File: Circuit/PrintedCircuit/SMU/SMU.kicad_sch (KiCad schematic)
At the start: 20 parts, among them J1 Conn_01x07_Pin, J2 Conn_01x03_Pin, U1 MCP4922, U2 MCP1501-20xCH, U6 MCP3204

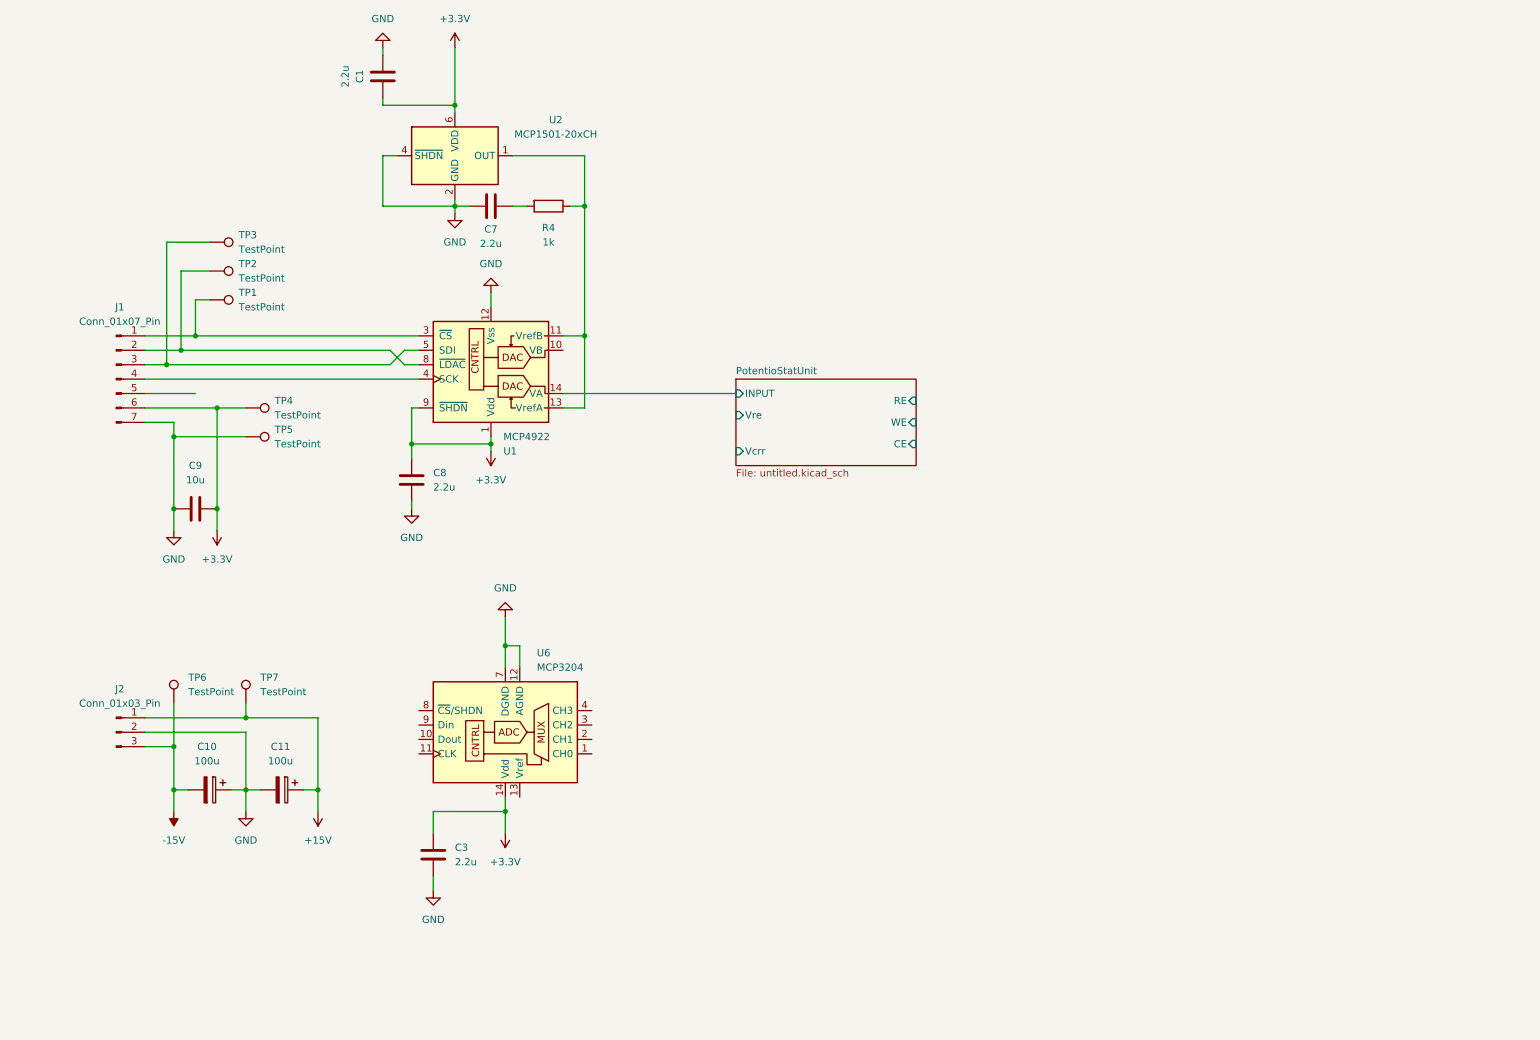
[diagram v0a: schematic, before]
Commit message: 保護回路のシミュレーションを追加
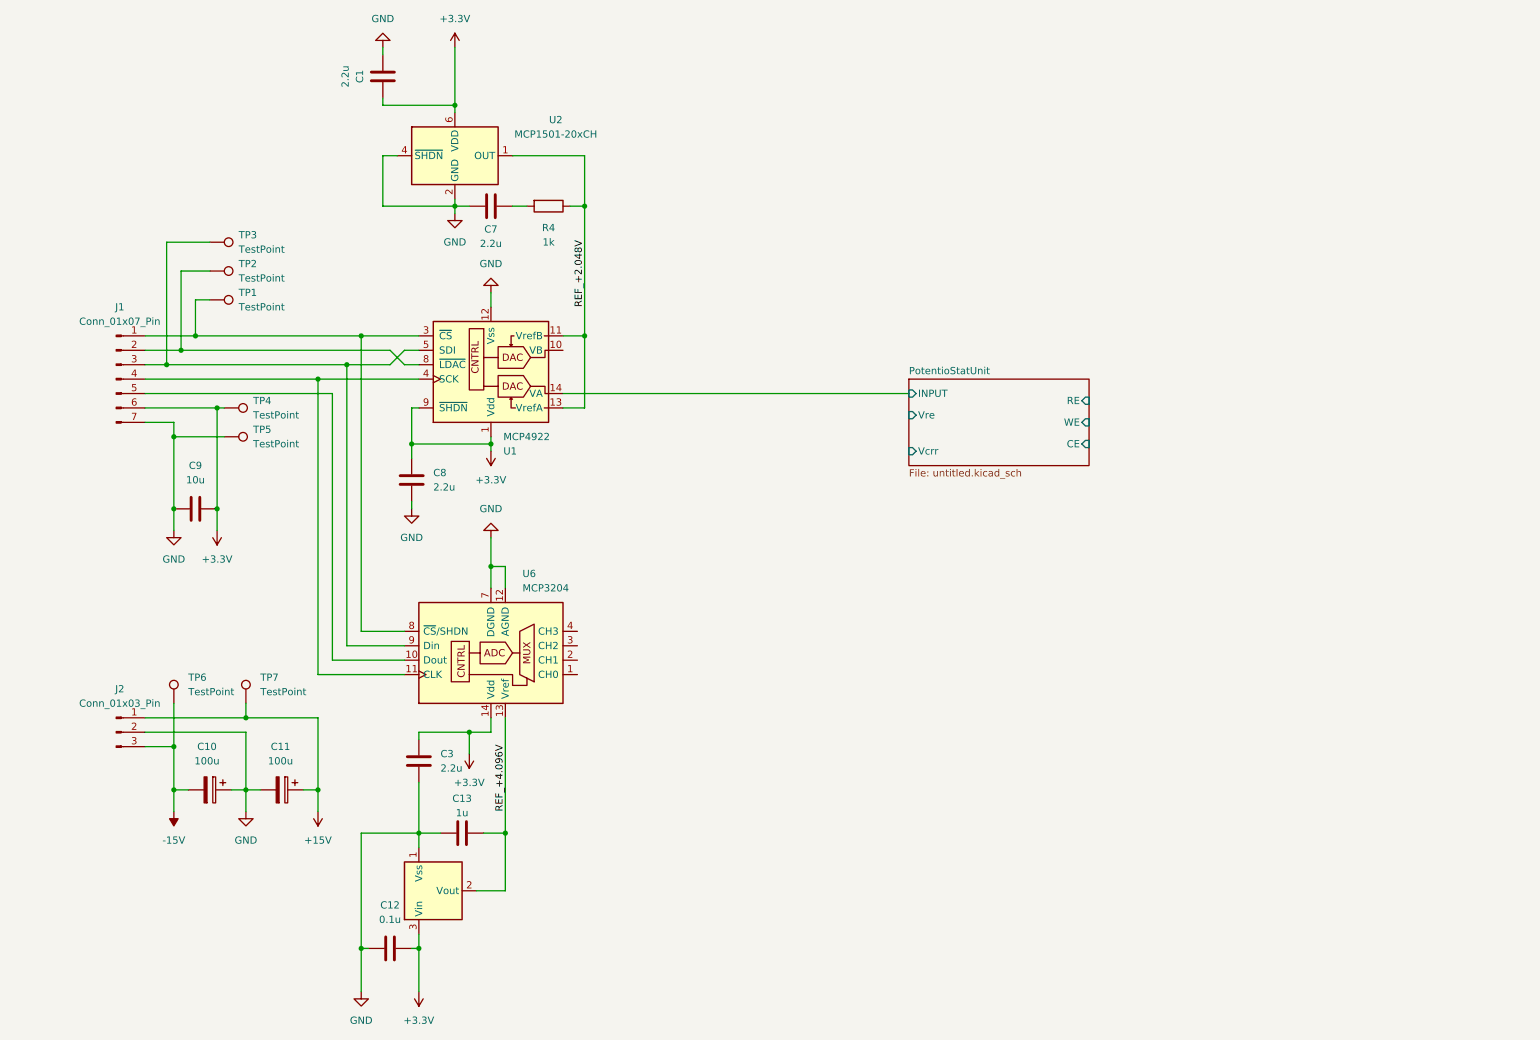
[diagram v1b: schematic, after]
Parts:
- added C12: 0.1u, symbol Device:C
- added C13: 1u, symbol Device:C
- added U7: MCP1541-TO, Package_TO_SOT_THT:TO-92_Inline, symbol Reference_Voltage:MCP1541-TO
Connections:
- net +3.3V: now also C12.2, U7.3 (Vin)
- net GND: now also C12.1, C13.1, U7.1 (Vss)
- net at U6.10 (Dout): now also J1.5 (Pin_5)
- net at U6.11 (CLK): now also J1.4 (Pin_4), U1.4 (SCK)
- net REF_+4.096V: now reaches U6.13 (Vref)
- net REF_+4.096V: now also C13.2, U7.2 (Vout)
- net at U6.8 (~{CS}/SHDN): now also J1.1 (Pin_1), TP1.1, U1.3 (~{CS})
- net at U6.9 (Din): now also J1.3 (Pin_3), TP3.1, U1.5 (SDI)
- net REF_+2.048V: now reaches R4.1, U1.11 (VrefB), U1.13 (VrefA), U2.1 (OUT)
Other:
- moved on the sheet: C3, TP4, TP5, U6

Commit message: SMUのプリント基板回路図完成
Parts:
- removed J1: Conn_01x07_Pin, symbol Connector:Conn_01x07_Pin
- added J1: Conn_01x08_Pin, symbol Connector:Conn_01x08_Pin
- added J3, J4, J5, J6: Conn_Coaxial, symbol Connector:Conn_Coaxial
- added SW1, SW2: SW_SPDT, symbol Switch:SW_SPDT
- added TP8: SPI_SCK, symbol Connector:TestPoint
- added TP9: SPI_RX, symbol Connector:TestPoint
- TP1: value TestPoint -> CS0
- TP2: value TestPoint -> CS1
- TP3: value TestPoint -> SPI_TX
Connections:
- net +3.3V: now also J1.7 (Pin_7)
- net GND: now also J1.8 (Pin_8)
- net PotentioStatUnit/CE: now also J5.2 (Ext), J6.2 (Ext)
- net PotentioStatUnit/RE: now also J5.1 (In), SW2.1 (A)
- net PotentioStatUnit/WE: now also SW2.2 (B)
- net 反転回路/OUTPUT: now reaches U6.1 (CH0)
- net at U6.10 (Dout): now also J1.6 (Pin_6), TP9.1
- net at U1.4 (SCK), U6.11 (CLK): now also J1.5 (Pin_5), TP8.1
- net 反転回路1/OUTPUT: now reaches U6.2 (CH1)
- net at TP1.1, U1.3 (~{CS}): now also J1.1 (Pin_1); no longer U6.8 (~{CS}/SHDN)
- net at TP3.1, U1.5 (SDI), U6.9 (Din): now also J1.4 (Pin_4)
- net at TP2.1: now also U6.8 (~{CS}/SHDN), J1.2 (Pin_2); no longer U1.8 (~{LDAC})
- net PotentioStatUnit1/INPUT: now reaches U1.10 (VB)
- new net: J6.1 (In), SW2.3 (C)
- new net: J4.1 (In), SW1.3 (C)
- new net: J1.3 (Pin_3), U1.8 (~{LDAC})
- new net PotentioStatUnit1/CE: J3.2 (Ext), J4.2 (Ext)
- new net PotentioStatUnit1/RE: J3.1 (In), SW1.1 (A)
- new net PotentioStatUnit1/WE: SW1.2 (B)
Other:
- added sheet PotentioStatUnit1 (untitled.kicad_sch)
- added sheet 反転回路 (Inverting.kicad_sch)
- added sheet 反転回路1 (Inverting.kicad_sch)
- moved on the sheet: C9, TP4, TP5

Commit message: フットプリント設定
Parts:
- removed TP7: TestPoint, symbol Connector:TestPoint
- removed TP8: SPI_SCK, symbol Connector:TestPoint
- removed TP9: SPI_RX, symbol Connector:TestPoint
- added J1: Conn_01x07_Pin, Connector_PinHeader_2.54mm:PinHeader_1x08_P2.54mm_Vertical, symbol Connector:Conn_01x07_Pin
- C1: footprint (none) -> Capacitor_SMD:C_0603_1608Metric_Pad1.08x0.95mm_HandSolder
- C2: renamed from C7; footprint (none) -> Capacitor_SMD:C_0603_1608Metric_Pad1.08x0.95mm_HandSolder
- C3: renamed from C8; footprint (none) -> Capacitor_SMD:C_0603_1608Metric_Pad1.08x0.95mm_HandSolder
- C4: renamed from C9; footprint (none) -> Capacitor_SMD:C_0603_1608Metric_Pad1.08x0.95mm_HandSolder
- C5: renamed from C10; footprint (none) -> Capacitor_SMD:C_0603_1608Metric_Pad1.08x0.95mm_HandSolder
- C6: renamed from C11; footprint (none) -> Capacitor_SMD:C_0603_1608Metric_Pad1.08x0.95mm_HandSolder
- C7: renamed from C3; footprint (none) -> Capacitor_SMD:C_0603_1608Metric_Pad1.08x0.95mm_HandSolder
- C8: renamed from C13; footprint (none) -> Capacitor_SMD:C_0603_1608Metric_Pad1.08x0.95mm_HandSolder
- C9: renamed from C12; footprint (none) -> Capacitor_SMD:C_0603_1608Metric_Pad1.08x0.95mm_HandSolder
- J2: renamed from J1; footprint (none) -> Connector_JST:JST_XH_B7B-XH-A_1x07_P2.50mm_Vertical
- J3, J4, J5: footprint (none) -> Connector_Coaxial:BNC_Amphenol_B6252HB-NPP3G-50_Horizontal
- J6: renamed from J2; footprint (none) -> Connector_JST:JST_XH_B3B-XH-A_1x03_P2.50mm_Vertical
- J7: renamed from J6; footprint (none) -> Connector_Coaxial:BNC_Amphenol_B6252HB-NPP3G-50_Horizontal
- R1: renamed from R4; footprint (none) -> Resistor_SMD:R_0603_1608Metric_Pad0.98x0.95mm_HandSolder
- SW1, SW2: footprint (none) -> Button_Switch_THT:SW_Slide-03_Wuerth-WS-SLTV_10x2.5x6.4_P2.54mm
- TP1: value CS0 -> TestPoint; footprint (none) -> Connector_PinHeader_2.54mm:PinHeader_1x01_P2.54mm_Vertical
- TP2: value CS1 -> TestPoint; footprint (none) -> Connector_PinHeader_2.54mm:PinHeader_1x01_P2.54mm_Vertical
- TP3: value SPI_TX -> TestPoint; footprint (none) -> Connector_PinHeader_2.54mm:PinHeader_1x01_P2.54mm_Vertical
- TP4, TP5, TP6: footprint (none) -> Connector_PinHeader_2.54mm:PinHeader_1x01_P2.54mm_Vertical
- U2: renamed from U1; footprint (none) -> Package_DIP:DIP-14_W7.62mm
- U3: renamed from U6; footprint (none) -> Package_DIP:DIP-14_W7.62mm
- renumbered U2 to U1, U7 to U4
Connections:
- net +15V: now also J1.6 (Pin_6)
- net +3.3V: now also J1.4 (Pin_4); no longer TP4.1
- net -15V: now also J1.7 (Pin_7); no longer TP6.1
- net GND: now also J1.5 (Pin_5); no longer TP5.1
- net PotentioStatUnit/INPUT: now also TP2.1
- net PotentioStatUnit/Vcrr: now also TP4.1
- net PotentioStatUnit1/INPUT: now also TP1.1
- net PotentioStatUnit1/Vcrr: now also TP6.1
- net 反転回路/OUTPUT: now also TP3.1
- net 反転回路1/OUTPUT: now also TP5.1
- net at J2.6 (Pin_6), U3.10 (Dout): now also J1.3 (Pin_3)
- net at J2.5 (Pin_5), U2.4 (SCK), U3.11 (CLK): now also J1.2 (Pin_2)
- net at J2.2 (Pin_2), U3.8 (~{CS}/SHDN): no longer TP2.1
- net at J2.4 (Pin_4), U2.5 (SDI), U3.9 (Din): now also J1.1 (Pin_1); no longer TP3.1
- net at J2.1 (Pin_1), U2.3 (~{CS}): no longer TP1.1
- no-connect marks 0 -> 2
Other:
- note added: "+ RE (SMU:-) - CE (SMU:+)"
- note added: "+ WE (SMU:NC) - CE (SMU:-)"
- note added: "1: SMUmode 3: PGSmode"
- note added: "J1 - 1: SPI_TX 2: SPI_SCK 3: SPI_RX 4: +3.3V 5: GND 6: +15V 7: -15V"
- note added: "TP1: INPUT_B TP2: INPUT_A TP3: Vcrr_INV_A TP4: Vcrr_A TP5: Vcrr_INV_B TP6: Vcrr_B"
- moved on the sheet: C5, C6, J6

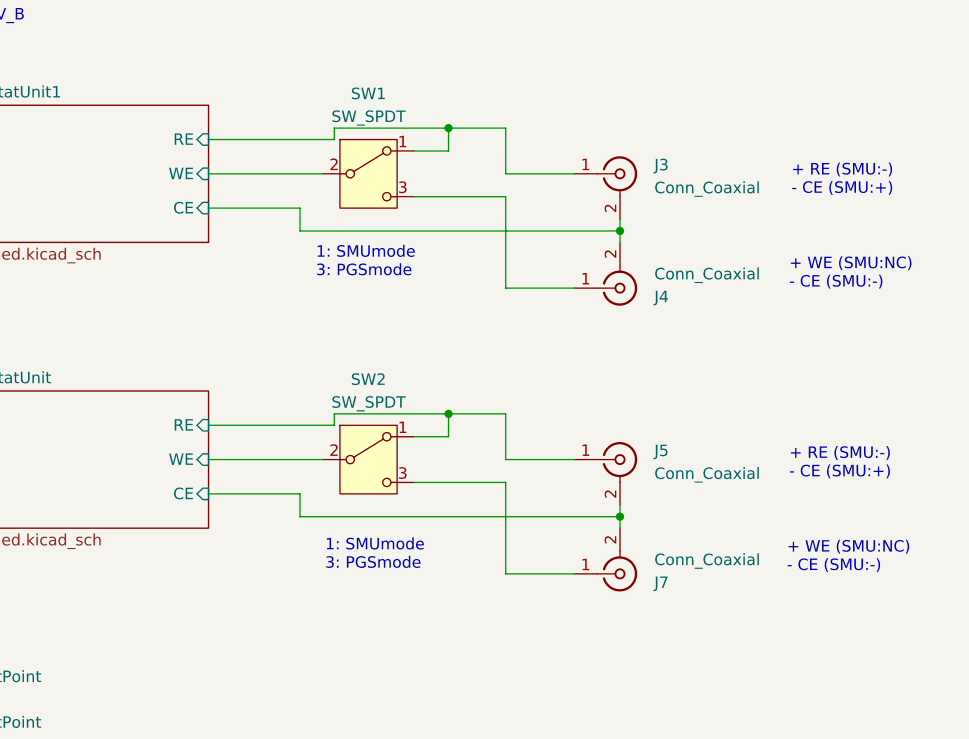
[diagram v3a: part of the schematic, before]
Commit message: WEとCEが逆転していた不具合を修正
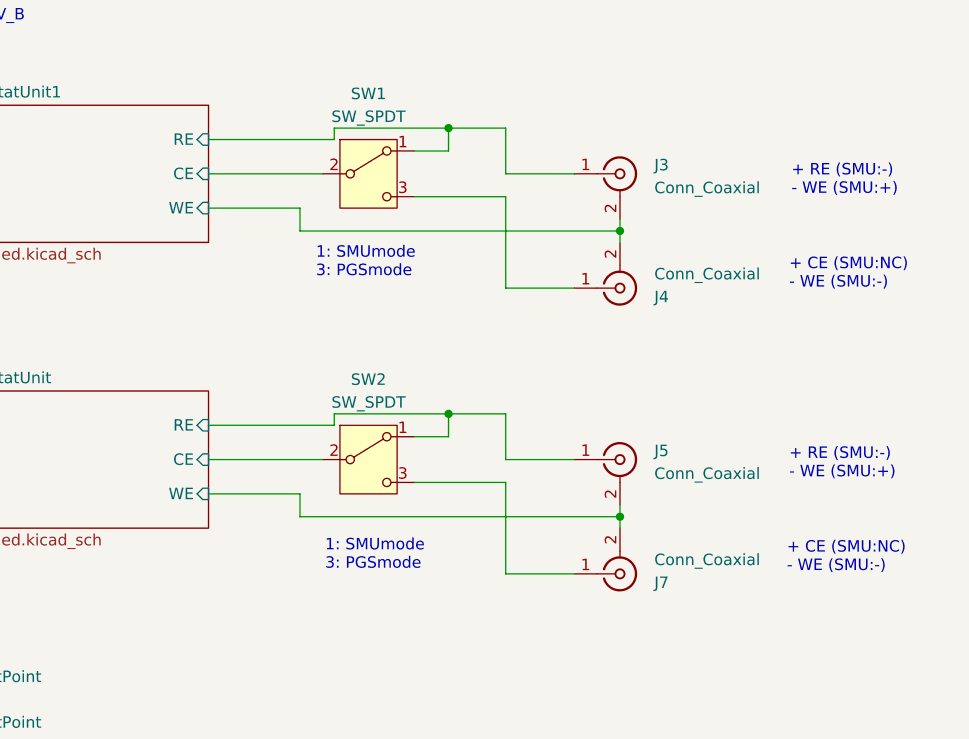
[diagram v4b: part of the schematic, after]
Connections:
- net PotentioStatUnit/CE: now also SW2.2 (B); no longer J5.2 (Ext), J7.2 (Ext)
- net PotentioStatUnit/WE: now also J5.2 (Ext), J7.2 (Ext); no longer SW2.2 (B)
- net PotentioStatUnit1/CE: now also SW1.2 (B); no longer J3.2 (Ext), J4.2 (Ext)
- net PotentioStatUnit1/WE: now also J3.2 (Ext), J4.2 (Ext); no longer SW1.2 (B)
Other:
- note added: "+ CE (SMU:NC) - WE (SMU:-)"
- note added: "+ RE (SMU:-) - WE (SMU:+)"
- note removed: "+ RE (SMU:-) - CE (SMU:+)"
- note removed: "+ WE (SMU:NC) - CE (SMU:-)"
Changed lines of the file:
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@@
 	(wire
 		(pts
+			(xy 195.58 93.98) (xy 208.28 93.98)
+		)
+		(stroke
+			(width 0)
+			(type default)
+		)
+	)
+	(wire
+		(pts
 			(xy 81.28 92.71) (xy 81.28 90.17)
 		)
@@
 	(wire
 		(pts
-			(xy 195.58 97.79) (xy 205.74 97.79)
-		)
-		(stroke
-			(width 0)
-			(type default)
-		)
-	)
-	(wire
-		(pts
 			(xy 88.9 48.26) (xy 88.9 46.99)
 		)
@@
 	(wire
 		(pts
-			(xy 195.58 93.98) (xy 208.28 93.98)
-		)
-		(stroke
-			(width 0)
-			(type default)
-		)
-	)
-	(wire
-		(pts
 			(xy 148.59 60.96) (xy 151.13 60.96)
 		)
@@
 	(wire
 		(pts
-			(xy 195.58 125.73) (xy 208.28 125.73)
-		)
-		(stroke
-			(width 0)
-			(type default)
-		)
-	)
-	(wire
-		(pts
 			(xy 120.65 128.27) (xy 120.65 153.67)
 		)
@@
 	(wire
 		(pts
-			(xy 195.58 129.54) (xy 205.74 129.54)
-		)
-		(stroke
-			(width 0)
-			(type default)
-		)
-	)
-	(wire
-		(pts
 			(xy 24.13 129.54) (xy 41.91 129.54)
 		)
@@
 	(wire
 		(pts
+			(xy 195.58 97.79) (xy 205.74 97.79)
+		)
+		(stroke
+			(width 0)
+			(type default)
+		)
+	)
+	(wire
+		(pts
 			(xy 123.19 148.59) (xy 125.73 148.59)
 		)
@@
 	(wire
 		(pts
+			(xy 195.58 129.54) (xy 205.74 129.54)
+		)
+		(stroke
+			(width 0)
+			(type default)
+		)
+	)
+	(wire
+		(pts
 			(xy 31.75 35.56) (xy 59.69 35.56)
 		)
@@
 	(wire
 		(pts
+			(xy 195.58 125.73) (xy 208.28 125.73)
+		)
+		(stroke
+			(width 0)
+			(type default)
+		)
+	)
+	(wire
+		(pts
 			(xy 97.79 138.43) (xy 97.79 158.75)
 		)
@@
 		)
 	)
-	(text "+ RE (SMU:-)\n- CE (SMU:+)"
+	(text "+ RE (SMU:-)\n- WE (SMU:+)"
 		(exclude_from_sim no)
 		(at 260.096 124.46 0)
@@
 		)
 	)
-	(text "+ WE (SMU:NC)\n- CE (SMU:-)"
+	(text "+ CE (SMU:NC)\n- WE (SMU:-)"
 		(exclude_from_sim no)
 		(at 259.842 134.874 0)
@@
 		)
 	)
-	(text "+ WE (SMU:NC)\n- CE (SMU:-)"
+	(text "+ CE (SMU:NC)\n- WE (SMU:-)"
 		(exclude_from_sim no)
 		(at 260.096 103.378 0)
@@
 		)
 	)
-	(text "+ RE (SMU:-)\n- CE (SMU:+)"
+	(text "+ RE (SMU:-)\n- WE (SMU:+)"
 		(exclude_from_sim no)
 		(at 260.35 92.964 0)
@@
 		)
 		(pin "CE" input
-			(at 195.58 129.54 0)
+			(at 195.58 125.73 0)
 			(effects
 				(font
@@
 		)
 		(pin "WE" input
-			(at 195.58 125.73 0)
+			(at 195.58 129.54 0)
 			(effects
 				(font
@@
 		)
 		(pin "CE" input
-			(at 195.58 97.79 0)
+			(at 195.58 93.98 0)
 			(effects
 				(font
@@
 		)
 		(pin "WE" input
-			(at 195.58 93.98 0)
+			(at 195.58 97.79 0)
 			(effects
 				(font
